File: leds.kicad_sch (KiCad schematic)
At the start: 12 parts

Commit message: final touches
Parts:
- C31, C32, C33, C34, C35, C36: value 0.1uF -> 100nF
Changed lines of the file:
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@@
 			)
 		)
-		(property "Value" "0.1uF"
+		(property "Value" "100nF"
 			(at 105.156 75.184 0)
 			(effects
@@
 			)
 		)
-		(property "Value" "0.1uF"
+		(property "Value" "100nF"
 			(at 235.966 84.074 0)
 			(effects
@@
 			)
 		)
-		(property "Value" "0.1uF"
+		(property "Value" "100nF"
 			(at 224.536 75.184 0)
 			(effects
@@
 			)
 		)
-		(property "Value" "0.1uF"
+		(property "Value" "100nF"
 			(at 145.796 75.184 0)
 			(effects
@@
 			)
 		)
-		(property "Value" "0.1uF"
+		(property "Value" "100nF"
 			(at 36.576 84.074 0)
 			(effects
@@
 			)
 		)
-		(property "Value" "0.1uF"
+		(property "Value" "100nF"
 			(at 185.166 75.184 0)
 			(effects

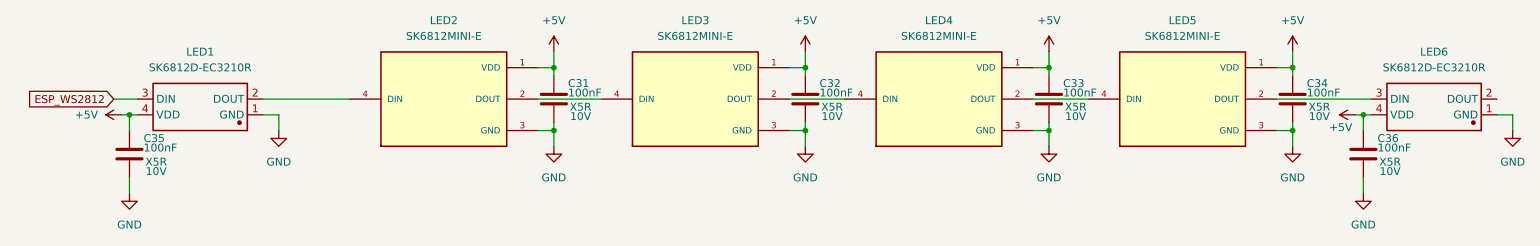
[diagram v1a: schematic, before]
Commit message: modifications for manufacturing
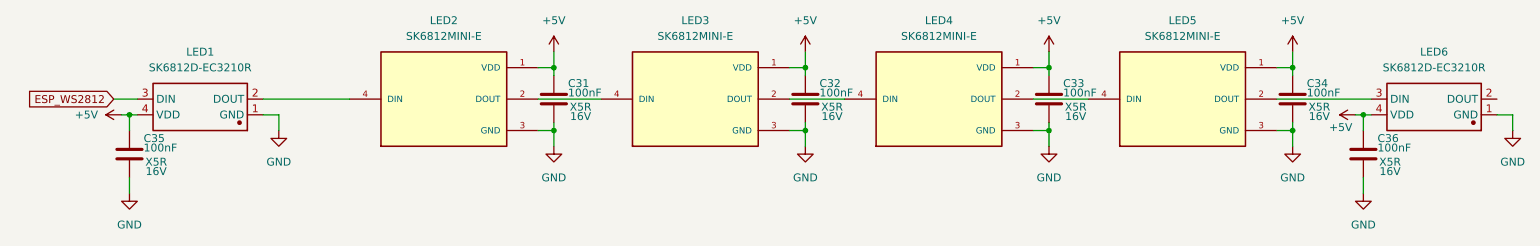
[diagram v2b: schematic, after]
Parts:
- C31, C32, C33, C34, C35, C36: Supplier Part (none) -> C1525; Voltage 10V -> 16V
- LED1, LED6: MANUFACTURER (none) -> OPSCO Optoelectronics; MP (none) -> SK6812D-EC3210R
- LED2, LED3, LED4, LED5: MANUFACTURER DONGGUANG OPSCO -> OPSCO Optoelectronics; MP SK6812-E -> SK6812MINI-E; Supplier Part (none) -> C5149201
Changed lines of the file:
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@@
 			)
 		)
-		(property "Voltage" "10V"
+		(property "Voltage" "16V"
 			(at 107.188 78.994 0)
 			(effects
@@
 		)
 		(property "Function" "LED"
+			(at 102.87 76.2 0)
+			(effects
+				(font
+					(size 1.27 1.27)
+				)
+				(hide yes)
+			)
+		)
+		(property "Supplier Part" "C1525"
 			(at 102.87 76.2 0)
 			(effects
@@
 			)
 		)
-		(property "Voltage" "10V"
+		(property "Voltage" "16V"
 			(at 237.998 87.884 0)
 			(effects
@@
 		)
 		(property "Function" "LED"
+			(at 233.68 85.09 0)
+			(effects
+				(font
+					(size 1.27 1.27)
+				)
+				(hide yes)
+			)
+		)
+		(property "Supplier Part" "C1525"
 			(at 233.68 85.09 0)
 			(effects
@@
 			)
 		)
-		(property "MP" "SK6812-E"
+		(property "MP" "SK6812MINI-E"
 			(at 85.09 76.2 0)
 			(effects
@@
 			)
 		)
-		(property "MANUFACTURER" "DONGGUANG OPSCO"
+		(property "MANUFACTURER" "OPSCO Optoelectronics"
 			(at 85.09 76.2 0)
 			(effects
@@
 		)
 		(property "Function" "LED"
+			(at 85.09 76.2 0)
+			(effects
+				(font
+					(size 1.27 1.27)
+				)
+				(hide yes)
+			)
+		)
+		(property "Supplier Part" "C5149201"
 			(at 85.09 76.2 0)
 			(effects
@@
 			)
 		)
-		(property "MP" "SK6812-E"
+		(property "MP" "SK6812MINI-E"
 			(at 125.73 76.2 0)
 			(effects
@@
 			)
 		)
-		(property "MANUFACTURER" "DONGGUANG OPSCO"
+		(property "MANUFACTURER" "OPSCO Optoelectronics"
 			(at 125.73 76.2 0)
 			(effects
@@
 		)
 		(property "Function" "LED"
+			(at 125.73 76.2 0)
+			(effects
+				(font
+					(size 1.27 1.27)
+				)
+				(hide yes)
+			)
+		)
+		(property "Supplier Part" "C5149201"
 			(at 125.73 76.2 0)
 			(effects
@@
 			)
 		)
-		(property "MP" "SK6812-E"
+		(property "MP" "SK6812MINI-E"
 			(at 165.1 76.2 0)
 			(effects
@@
 			)
 		)
-		(property "MANUFACTURER" "DONGGUANG OPSCO"
+		(property "MANUFACTURER" "OPSCO Optoelectronics"
 			(at 165.1 76.2 0)
 			(effects
@@
 		)
 		(property "Function" "LED"
+			(at 165.1 76.2 0)
+			(effects
+				(font
+					(size 1.27 1.27)
+				)
+				(hide yes)
+			)
+		)
+		(property "Supplier Part" "C5149201"
 			(at 165.1 76.2 0)
 			(effects
@@
 			)
 		)
-		(property "Voltage" "10V"
+		(property "Voltage" "16V"
 			(at 226.568 78.994 0)
 			(effects
@@
 		)
 		(property "Function" "LED"
+			(at 222.25 76.2 0)
+			(effects
+				(font
+					(size 1.27 1.27)
+				)
+				(hide yes)
+			)
+		)
+		(property "Supplier Part" "C1525"
 			(at 222.25 76.2 0)
 			(effects
@@
 			)
 		)
+		(property "MANUFACTURER" "OPSCO Optoelectronics"
+			(at 45.72 77.47 0)
+			(effects
+				(font
+					(size 1.27 1.27)
+				)
+				(hide yes)
+			)
+		)
+		(property "MP" "SK6812D-EC3210R"
+			(at 45.72 77.47 0)
+			(effects
+				(font
+					(size 1.27 1.27)
+				)
+				(hide yes)
+			)
+		)
 		(pin "2"
 		)
@@
 			)
 		)
+		(property "MANUFACTURER" "OPSCO Optoelectronics"
+			(at 245.11 77.47 0)
+			(effects
+				(font
+					(size 1.27 1.27)
+				)
+				(hide yes)
+			)
+		)
+		(property "MP" "SK6812D-EC3210R"
+			(at 245.11 77.47 0)
+			(effects
+				(font
+					(size 1.27 1.27)
+				)
+				(hide yes)
+			)
+		)
 		(pin "3"
 		)
@@
 			)
 		)
-		(property "MP" "SK6812-E"
+		(property "MP" "SK6812MINI-E"
 			(at 204.47 76.2 0)
 			(effects
@@
 			)
 		)
-		(property "MANUFACTURER" "DONGGUANG OPSCO"
+		(property "MANUFACTURER" "OPSCO Optoelectronics"
 			(at 204.47 76.2 0)
 			(effects
@@
 		)
 		(property "Function" "LED"
+			(at 204.47 76.2 0)
+			(effects
+				(font
+					(size 1.27 1.27)
+				)
+				(hide yes)
+			)
+		)
+		(property "Supplier Part" "C5149201"
 			(at 204.47 76.2 0)
 			(effects
@@
 			)
 		)
-		(property "Voltage" "10V"
+		(property "Voltage" "16V"
 			(at 147.828 78.994 0)
 			(effects
@@
 		)
 		(property "Function" "LED"
+			(at 143.51 76.2 0)
+			(effects
+				(font
+					(size 1.27 1.27)
+				)
+				(hide yes)
+			)
+		)
+		(property "Supplier Part" "C1525"
 			(at 143.51 76.2 0)
 			(effects
@@
 			)
 		)
-		(property "Voltage" "10V"
+		(property "Voltage" "16V"
 			(at 38.608 87.884 0)
 			(effects
@@
 		)
 		(property "Function" "LED"
+			(at 34.29 85.09 0)
+			(effects
+				(font
+					(size 1.27 1.27)
+				)
+				(hide yes)
+			)
+		)
+		(property "Supplier Part" "C1525"
 			(at 34.29 85.09 0)
 			(effects
@@
 			)
 		)
-		(property "Voltage" "10V"
+		(property "Voltage" "16V"
 			(at 187.198 78.994 0)
 			(effects
@@
 			(at 182.88 76.2 0)
 			(effects
+				(font
+					(size 1.27 1.27)
+				)
+				(hide yes)
+			)
+		)
+		(property "Supplier Part" "C1525"
+			(at 182.88 76.2 0)
+			(effects

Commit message: modifications for manufacturing
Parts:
- LED1, LED6: Manufacturer 欧思科光电 -> OPSCO Optoelectronics
- LED2, LED3, LED4, LED5: Manufacturer (none) -> OPSCO Optoelectronics; Manufacturer Part (none) -> SK6812MINI-E
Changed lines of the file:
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@@
+			)
+		)
+		(property "Manufacturer" "OPSCO Optoelectronics"
+			(at 85.09 76.2 0)
+			(effects
+				(font
+					(size 1.27 1.27)
+				)
+				(hide yes)
+			)
+		)
+		(property "Manufacturer Part" "SK6812MINI-E"
+			(at 85.09 76.2 0)
+			(effects
+				(font
+					(size 1.27 1.27)
+				)
+				(hide yes)
 			)
 		)
@@
 			)
 		)
+		(property "Manufacturer" "OPSCO Optoelectronics"
+			(at 125.73 76.2 0)
+			(effects
+				(font
+					(size 1.27 1.27)
+				)
+				(hide yes)
+			)
+		)
+		(property "Manufacturer Part" "SK6812MINI-E"
+			(at 125.73 76.2 0)
+			(effects
+				(font
+					(size 1.27 1.27)
+				)
+				(hide yes)
+			)
+		)
 		(pin "2"
 		)
@@
 			)
 		)
+		(property "Manufacturer" "OPSCO Optoelectronics"
+			(at 165.1 76.2 0)
+			(effects
+				(font
+					(size 1.27 1.27)
+				)
+				(hide yes)
+			)
+		)
+		(property "Manufacturer Part" "SK6812MINI-E"
+			(at 165.1 76.2 0)
+			(effects
+				(font
+					(size 1.27 1.27)
+				)
+				(hide yes)
+			)
+		)
 		(pin "2"
 		)
@@
 			)
 		)
-		(property "Manufacturer" "欧思科光电"
+		(property "Manufacturer" "OPSCO Optoelectronics"
 			(at 45.72 77.47 0)
 			(effects
@@
 			)
 		)
-		(property "Manufacturer" "欧思科光电"
+		(property "Manufacturer" "OPSCO Optoelectronics"
 			(at 245.11 77.47 0)
 			(effects
@@
 			(at 204.47 76.2 0)
 			(effects
+				(font
+					(size 1.27 1.27)
+				)
+				(hide yes)
+			)
+		)
+		(property "Manufacturer" "OPSCO Optoelectronics"
+			(at 204.47 76.2 0)
+			(effects
+				(font
+					(size 1.27 1.27)
+				)
+				(hide yes)
+			)
+		)
+		(property "Manufacturer Part" "SK6812MINI-E"
+			(at 204.47 76.2 0)
+			(effects

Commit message: modifications for manufacturing
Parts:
- C31, C32, C33, C34, C35, C36: LCSC Part # (none) -> C1525
- LED1, LED6: LCSC Part # (none) -> C2890041
- LED2, LED3, LED4, LED5: LCSC Part # (none) -> C5149201
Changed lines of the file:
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@@
+			)
+		)
+		(property "LCSC Part #" "C1525"
+			(at 102.87 76.2 0)
+			(effects
+				(font
+					(size 1.27 1.27)
+				)
+				(hide yes)
 			)
 		)
@@
 			)
 		)
+		(property "LCSC Part #" "C1525"
+			(at 233.68 85.09 0)
+			(effects
+				(font
+					(size 1.27 1.27)
+				)
+				(hide yes)
+			)
+		)
 		(pin "1"
 		)
@@
 			)
 		)
+		(property "LCSC Part #" "C5149201"
+			(at 85.09 76.2 0)
+			(effects
+				(font
+					(size 1.27 1.27)
+				)
+				(hide yes)
+			)
+		)
 		(pin "2"
 		)
@@
 			)
 		)
+		(property "LCSC Part #" "C5149201"
+			(at 125.73 76.2 0)
+			(effects
+				(font
+					(size 1.27 1.27)
+				)
+				(hide yes)
+			)
+		)
 		(pin "2"
 		)
@@
 			)
 		)
+		(property "LCSC Part #" "C5149201"
+			(at 165.1 76.2 0)
+			(effects
+				(font
+					(size 1.27 1.27)
+				)
+				(hide yes)
+			)
+		)
 		(pin "2"
 		)
@@
 		)
 		(property "Supplier Part" "C1525"
+			(at 222.25 76.2 0)
+			(effects
+				(font
+					(size 1.27 1.27)
+				)
+				(hide yes)
+			)
+		)
+		(property "LCSC Part #" "C1525"
 			(at 222.25 76.2 0)
 			(effects
@@
 			)
 		)
+		(property "LCSC Part #" "C2890041"
+			(at 45.72 77.47 0)
+			(effects
+				(font
+					(size 1.27 1.27)
+				)
+				(hide yes)
+			)
+		)
 		(pin "2"
 		)
@@
 			)
 		)
+		(property "LCSC Part #" "C2890041"
+			(at 245.11 77.47 0)
+			(effects
+				(font
+					(size 1.27 1.27)
+				)
+				(hide yes)
+			)
+		)
 		(pin "3"
 		)
@@
 			)
 		)
+		(property "LCSC Part #" "C5149201"
+			(at 204.47 76.2 0)
+			(effects
+				(font
+					(size 1.27 1.27)
+				)
+				(hide yes)
+			)
+		)
 		(pin "2"
 		)
@@
 			)
 		)
+		(property "LCSC Part #" "C1525"
+			(at 143.51 76.2 0)
+			(effects
+				(font
+					(size 1.27 1.27)
+				)
+				(hide yes)
+			)
+		)
 		(pin "1"
 		)
@@
 			)
 		)
+		(property "LCSC Part #" "C1525"
+			(at 34.29 85.09 0)
+			(effects
+				(font
+					(size 1.27 1.27)
+				)
+				(hide yes)
+			)
+		)
 		(pin "1"
 		)
@@
 			(at 182.88 76.2 0)
 			(effects
+				(font
+					(size 1.27 1.27)
+				)
+				(hide yes)
+			)
+		)
+		(property "LCSC Part #" "C1525"
+			(at 182.88 76.2 0)
+			(effects

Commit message: update for production
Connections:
- no-connect marks 0 -> 1
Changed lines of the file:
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@@
 		(color 0 0 0 0)
+	)
+	(no_connect
+		(at 255.27 76.2)
 	)
 	(wire

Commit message: complete redesign
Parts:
- LED2, LED3, LED4, LED5: value SK6812MINI-E -> SK6805-EC20; footprint Onju:SK6812MINI-E -> Onju:SK6805-EC20; Availability Not in stock -> (none); Check_prices https://www.snapeda.com/parts/SK6812-E/DONGGUANG+OPSCO+OPTO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 -> (none); Description_1 SK6812MINI-E is a smart LED control circuit and light emitt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 -> (none); LCSC Part # C5149201 -> C2890036; MANUFACTURER OPSCO Optoelectronics -> (none); MAXIMUM_PACKAGE_HEIGHT 0.84mm -> (none); MF DONGGUANG OPSCO OPTOELECTRONICS CO., LTD -> (none); MP SK6812MINI-E -> SK6805-EC20; Manufacturer Part SK6812MINI-E -> SK6805-EC20; PARTREV 2 -> (none); Package Package -> (none); Price None -> (none); STANDARD Manufacturer recommendations -> (none); SnapEDA_Link https://www.snapeda.com/parts/SK6812-E/DONGGUANG+OPSCO+OPTO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 -> (none); Supplier Part C5149201 -> C2890036
- renumbered C35 to C80, C31 to C81, C32 to C82, C33 to C83, C34 to C84, C36 to C85
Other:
- title: Nest mini drop in PCB replacement -> Drop in replacement PCB for Nest mini GEN2

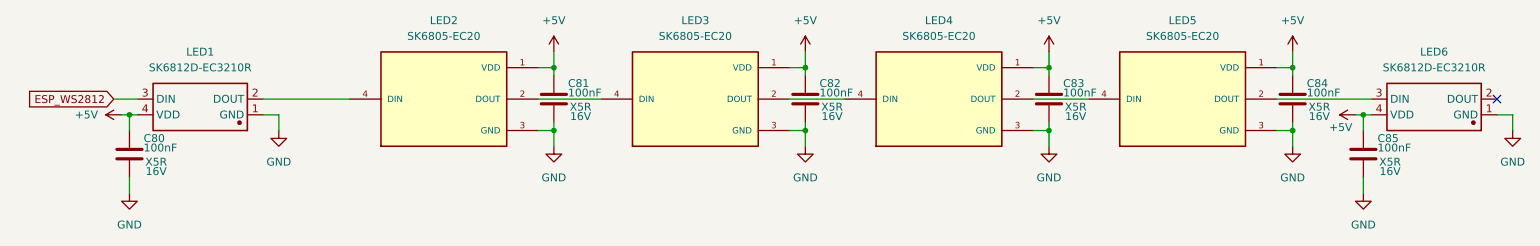
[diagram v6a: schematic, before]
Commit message: v2 hardware revision
MPR121 touch controller added to replace the esp32-s3 internal touch interface
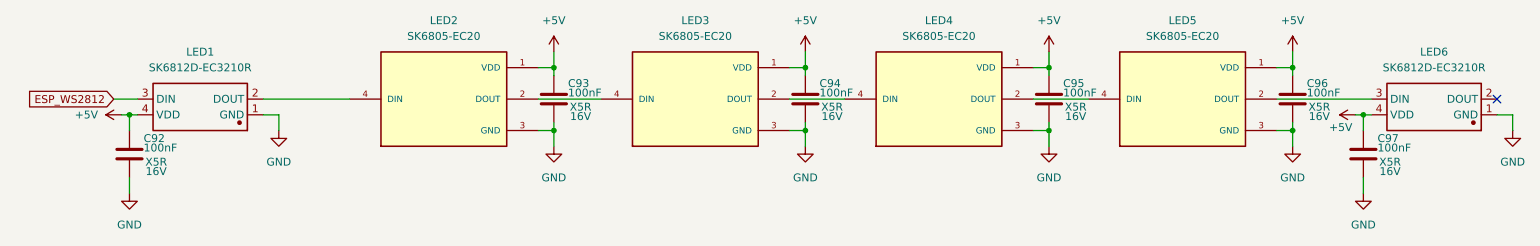
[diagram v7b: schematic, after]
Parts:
- renumbered C80 to C92, C81 to C93, C82 to C94, C83 to C95, C84 to C96, C85 to C97
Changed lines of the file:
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@@
 		(dnp no)
 		(fields_autoplaced yes)
-		(property "Reference" "#PWR0157"
+		(property "Reference" "#PWR0182"
 			(at 182.88 72.39 0)
 			(effects
@@
 			(project ""
 				(path "/204e071a-14ed-47a0-be54-332ac2b951cf/18f90dfa-9bd7-48d0-80c5-47366522e296"
-					(reference "#PWR0157")
+					(reference "#PWR0182")
 					(unit 1)
 				)
@@
 		(on_board yes)
 		(dnp no)
-		(property "Reference" "C81"
+		(property "Reference" "C93"
 			(at 105.156 73.66 0)
 			(effects
@@
 			(project ""
 				(path "/204e071a-14ed-47a0-be54-332ac2b951cf/18f90dfa-9bd7-48d0-80c5-47366522e296"
-					(reference "C81")
+					(reference "C93")
 					(unit 1)
 				)
@@
 		(dnp no)
 		(fields_autoplaced yes)
-		(property "Reference" "#PWR0152"
+		(property "Reference" "#PWR0177"
 			(at 58.42 87.63 0)
 			(effects
@@
 			(project ""
 				(path "/204e071a-14ed-47a0-be54-332ac2b951cf/18f90dfa-9bd7-48d0-80c5-47366522e296"
-					(reference "#PWR0152")
+					(reference "#PWR0177")
 					(unit 1)
 				)
@@
 		(dnp no)
 		(fields_autoplaced yes)
-		(property "Reference" "#PWR0155"
+		(property "Reference" "#PWR0180"
 			(at 143.51 72.39 0)
 			(effects
@@
 			(project ""
 				(path "/204e071a-14ed-47a0-be54-332ac2b951cf/18f90dfa-9bd7-48d0-80c5-47366522e296"
-					(reference "#PWR0155")
+					(reference "#PWR0180")
 					(unit 1)
 				)
@@
 		(on_board yes)
 		(dnp no)
-		(property "Reference" "C85"
+		(property "Reference" "C97"
 			(at 235.966 82.55 0)
 			(effects
@@
 			(project "OBJ_PCB_onju_by_imike78_2025-05-11"
 				(path "/204e071a-14ed-47a0-be54-332ac2b951cf/18f90dfa-9bd7-48d0-80c5-47366522e296"
-					(reference "C85")
+					(reference "C97")
 					(unit 1)
 				)
@@
 		(dnp no)
 		(fields_autoplaced yes)
-		(property "Reference" "#PWR0163"
+		(property "Reference" "#PWR0188"
 			(at 257.81 87.63 0)
 			(effects
@@
 			(project ""
 				(path "/204e071a-14ed-47a0-be54-332ac2b951cf/18f90dfa-9bd7-48d0-80c5-47366522e296"
-					(reference "#PWR0163")
+					(reference "#PWR0188")
 					(unit 1)
 				)
@@
 		(dnp no)
 		(fields_autoplaced yes)
-		(property "Reference" "#PWR0160"
+		(property "Reference" "#PWR0185"
 			(at 222.25 90.17 0)
 			(effects
@@
 			(project ""
 				(path "/204e071a-14ed-47a0-be54-332ac2b951cf/18f90dfa-9bd7-48d0-80c5-47366522e296"
-					(reference "#PWR0160")
+					(reference "#PWR0185")
 					(unit 1)
 				)
@@
 		(on_board yes)
 		(dnp no)
-		(property "Reference" "#PWR0161"
+		(property "Reference" "#PWR0186"
 			(at 236.22 78.74 0)
 			(effects
@@
 			(project ""
 				(path "/204e071a-14ed-47a0-be54-332ac2b951cf/18f90dfa-9bd7-48d0-80c5-47366522e296"
-					(reference "#PWR0161")
+					(reference "#PWR0186")
 					(unit 1)
 				)
@@
 		(on_board yes)
 		(dnp no)
-		(property "Reference" "C84"
+		(property "Reference" "C96"
 			(at 224.536 73.66 0)
 			(effects
@@
 			(project "OBJ_PCB_onju_by_imike78_2025-05-11"
 				(path "/204e071a-14ed-47a0-be54-332ac2b951cf/18f90dfa-9bd7-48d0-80c5-47366522e296"
-					(reference "C84")
+					(reference "C96")
 					(unit 1)
 				)
@@
 		(dnp no)
 		(fields_autoplaced yes)
-		(property "Reference" "#PWR0154"
+		(property "Reference" "#PWR0179"
 			(at 102.87 90.17 0)
 			(effects
@@
 			(project ""
 				(path "/204e071a-14ed-47a0-be54-332ac2b951cf/18f90dfa-9bd7-48d0-80c5-47366522e296"
-					(reference "#PWR0154")
+					(reference "#PWR0179")
 					(unit 1)
 				)
@@
 		(dnp no)
 		(fields_autoplaced yes)
-		(property "Reference" "#PWR0156"
+		(property "Reference" "#PWR0181"
 			(at 143.51 90.17 0)
 			(effects
@@
 			(project ""
 				(path "/204e071a-14ed-47a0-be54-332ac2b951cf/18f90dfa-9bd7-48d0-80c5-47366522e296"
-					(reference "#PWR0156")
+					(reference "#PWR0181")
 					(unit 1)
 				)
@@
 		(on_board yes)
 		(dnp no)
-		(property "Reference" "C82"
+		(property "Reference" "C94"
 			(at 145.796 73.66 0)
 			(effects
@@
 			(project "OBJ_PCB_onju_by_imike78_2025-05-11"
 				(path "/204e071a-14ed-47a0-be54-332ac2b951cf/18f90dfa-9bd7-48d0-80c5-47366522e296"
-					(reference "C82")
+					(reference "C94")
 					(unit 1)
 				)
@@
 		(dnp no)
 		(fields_autoplaced yes)
-		(property "Reference" "#PWR0153"
+		(property "Reference" "#PWR0178"
 			(at 102.87 72.39 0)
 			(effects
@@
 			(project ""
 				(path "/204e071a-14ed-47a0-be54-332ac2b951cf/18f90dfa-9bd7-48d0-80c5-47366522e296"
-					(reference "#PWR0153")
+					(reference "#PWR0178")
 					(unit 1)
 				)
@@
 		(dnp no)
 		(fields_autoplaced yes)
-		(property "Reference" "#PWR0150"
+		(property "Reference" "#PWR0175"
 			(at 36.83 78.74 0)
 			(effects
@@
 			(project ""
 				(path "/204e071a-14ed-47a0-be54-332ac2b951cf/18f90dfa-9bd7-48d0-80c5-47366522e296"
-					(reference "#PWR0150")
+					(reference "#PWR0175")
 					(unit 1)
 				)
@@
 		(dnp no)
 		(fields_autoplaced yes)
-		(property "Reference" "#PWR0151"
+		(property "Reference" "#PWR0176"
 			(at 34.29 97.79 0)
 			(effects
@@
 			(project ""
 				(path "/204e071a-14ed-47a0-be54-332ac2b951cf/18f90dfa-9bd7-48d0-80c5-47366522e296"
-					(reference "#PWR0151")
+					(reference "#PWR0176")
 					(unit 1)
 				)
@@
 		(dnp no)
 		(fields_autoplaced yes)
-		(property "Reference" "#PWR0159"
+		(property "Reference" "#PWR0184"
 			(at 222.25 72.39 0)
 			(effects
@@
 			(project ""
 				(path "/204e071a-14ed-47a0-be54-332ac2b951cf/18f90dfa-9bd7-48d0-80c5-47366522e296"
-					(reference "#PWR0159")
+					(reference "#PWR0184")
 					(unit 1)
 				)
@@
 		(on_board yes)
 		(dnp no)
-		(property "Reference" "C80"
+		(property "Reference" "C92"
 			(at 36.576 82.55 0)
 			(effects
@@
 			(project "OBJ_PCB_onju_by_imike78_2025-05-11"
 				(path "/204e071a-14ed-47a0-be54-332ac2b951cf/18f90dfa-9bd7-48d0-80c5-47366522e296"
-					(reference "C80")
+					(reference "C92")
 					(unit 1)
 				)
@@
 		(on_board yes)
 		(dnp no)
-		(property "Reference" "C83"
+		(property "Reference" "C95"
 			(at 185.166 73.66 0)
 			(effects
@@
 			(project "OBJ_PCB_onju_by_imike78_2025-05-11"
 				(path "/204e071a-14ed-47a0-be54-332ac2b951cf/18f90dfa-9bd7-48d0-80c5-47366522e296"
-					(reference "C83")
+					(reference "C95")
 					(unit 1)
 				)
@@
 		(dnp no)
 		(fields_autoplaced yes)
-		(property "Reference" "#PWR0162"
+		(property "Reference" "#PWR0187"
 			(at 233.68 97.79 0)
 			(effects
@@
 			(project ""
 				(path "/204e071a-14ed-47a0-be54-332ac2b951cf/18f90dfa-9bd7-48d0-80c5-47366522e296"
-					(reference "#PWR0162")
+					(reference "#PWR0187")
 					(unit 1)
 				)
@@
 		(dnp no)
 		(fields_autoplaced yes)
-		(property "Reference" "#PWR0158"
+		(property "Reference" "#PWR0183"
 			(at 182.88 90.17 0)
 			(effects
@@
 			(project ""
 				(path "/204e071a-14ed-47a0-be54-332ac2b951cf/18f90dfa-9bd7-48d0-80c5-47366522e296"
-					(reference "#PWR0158")
-					(unit 1)
-				)
+					(reference "#PWR0183")
+					(unit 1)
+				)
